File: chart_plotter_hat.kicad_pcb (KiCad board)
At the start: 4 copper layers, 65 x 56 mm, 41 parts, among them J1 Conn_01x06, J2 Conn_01x04, J3 40HAT, J4 Conn_01x04, J5 Conn_01x04, J6 Conn_01x02, J7 Conn_01x04, J8 Conn_02x03_Odd_Even, J9 Conn_01x03, Q1 DMG2305UX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

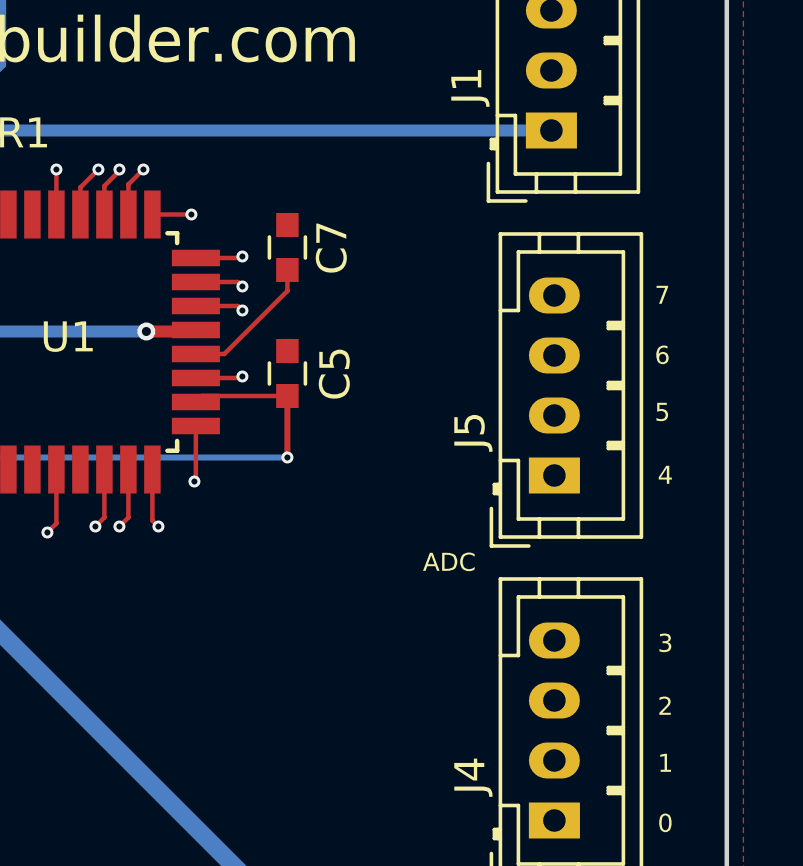
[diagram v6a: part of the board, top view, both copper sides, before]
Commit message: Added Inductor to AVCC
Added optional 12VBAT adc on A7
Changed P5V label to +5V
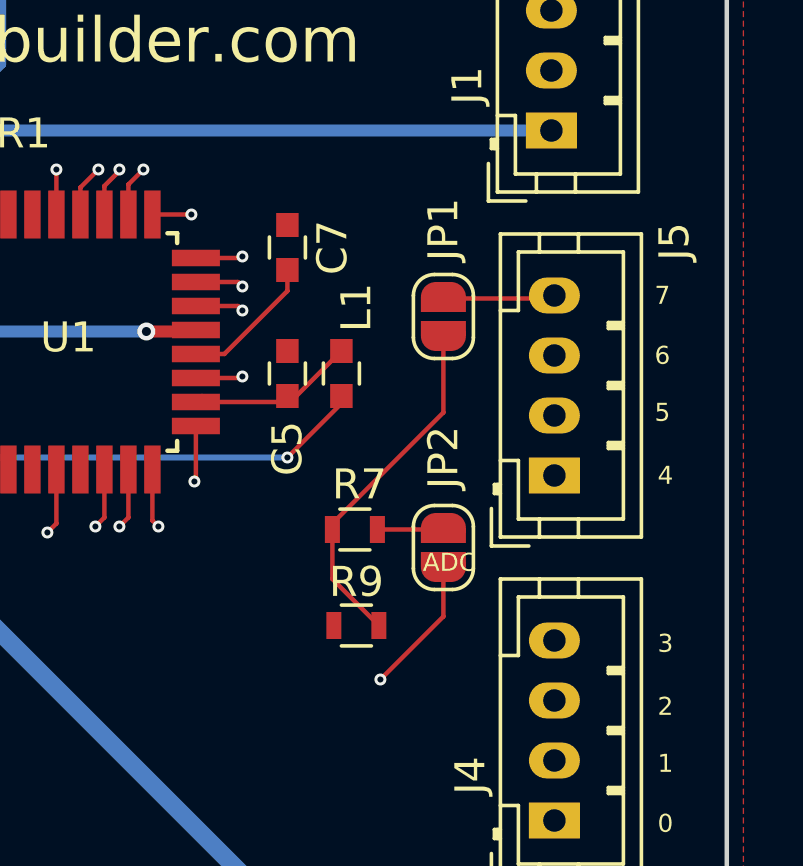
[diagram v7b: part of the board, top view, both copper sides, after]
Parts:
- added JP1: SolderJumper_2_Open, CustomComponents:SolderJumper-2_P1.3mm_Open_RoundedPad1.0x1.5mm, F.Cu at (134.1, 88.5)
- added JP2: SolderJumper_2_Open, CustomComponents:SolderJumper-2_P1.3mm_Open_RoundedPad1.0x1.5mm, F.Cu at (134.1, 96.2)
- added L1: 10uH, Capacitors_SMD:C_0603, F.Cu at (130.7, 90.4)
- added R7: 39K, Resistors_SMD:R_0603, F.Cu at (131.2, 95.6)
- added R9: 12K, Resistors_SMD:R_0603, F.Cu at (131.2, 98.8)
- J1: value Conn_01x06 -> JST PH
- J2, J4, J5, J7: value Conn_01x04 -> JST PH
- J6: value Conn_01x02 -> JST PH
- J9: value Conn_01x03 -> JST PH
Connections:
- net /P5V renamed +5V
- C5 pad 1: +3V3 -> Net-(C5-Pad1)
- U1 pad 18: +3V3 -> Net-(C5-Pad1)
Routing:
- net /12VBAT: track 39.7 -> 80.4 mm, vias 2 -> 3
- net Net-(JP1-Pad2): track 0.00 -> 11.8 mm
- net Net-(C5-Pad1): track 0.00 -> 6.12 mm
- net A7: track 12.2 -> 15.7 mm
- net +3V3: track 139.0 -> 136.7 mm
- net Net-(JP2-Pad1): track 0.00 -> 2.22 mm
